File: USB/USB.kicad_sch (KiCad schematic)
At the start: 18 parts, among them J1 USBC-4-0-CX90MW9-24P1, U2 ESDA25L, U3 USB SWITCH 2CHANNEL TS3USB221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, U6 usb-polarity-TUSB321RWBR

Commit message: added TVS protection and filtering to CC lines
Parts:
- added TVS4: (no value), SPIRIT-footprints:1-channel-TVS-choke-XDFN6_1P2X1P2_ONS, symbol SPIRIT-components:TVS-choke-1-pair-EMI8141
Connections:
- net CC1: now also TVS4.1 (D+IN); no longer J2.1, Module1.94 (CC1)
- net CC2: now also TVS4.2 (D-IN); no longer J3.1, Module1.96 (CC2)
- net GND: now also TVS4.3 (GND), TVS4.4 (GND)
- net CC1f-jumpered: now reaches J2.2, U6.1 (CC1)
- net CC1f-jumpered: now also Module1.94 (CC1)
- net CC2f-jumpered: now reaches J3.2, U6.2 (CC2)
- net CC2f-jumpered: now also Module1.96 (CC2)
- new net CC1f: J2.1, TVS4.6 (D+OUT)
- new net CC2f: J3.1, TVS4.5 (D-OUT)
- no-connect marks 22 -> 30

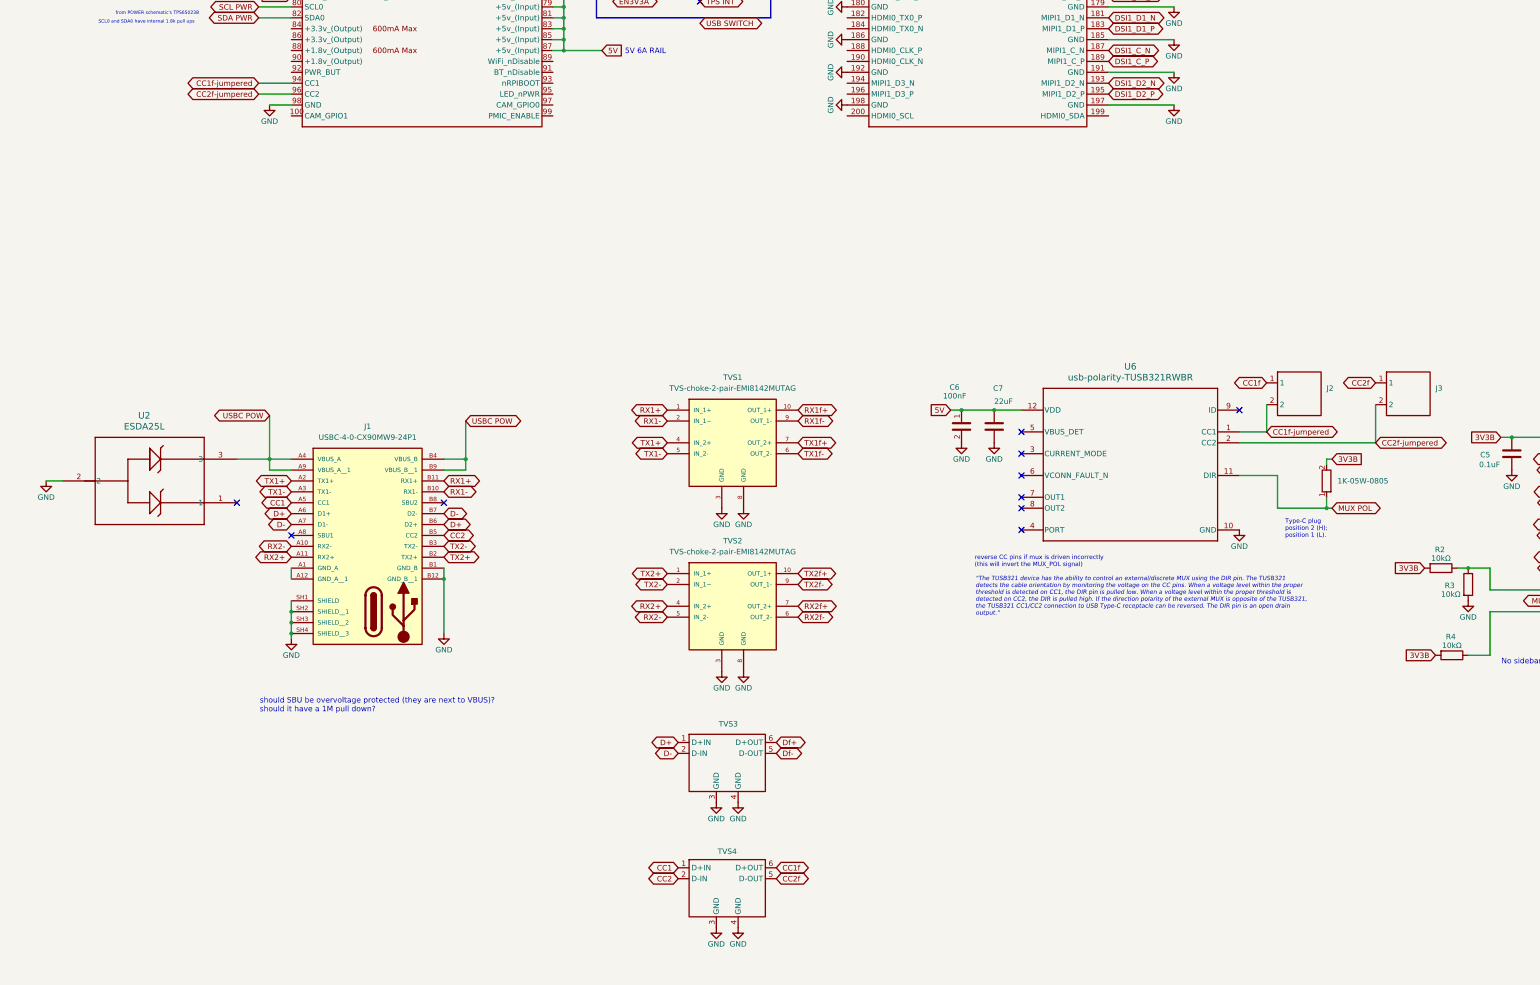
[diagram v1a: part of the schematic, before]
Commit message: fix TVS protection on CC lines
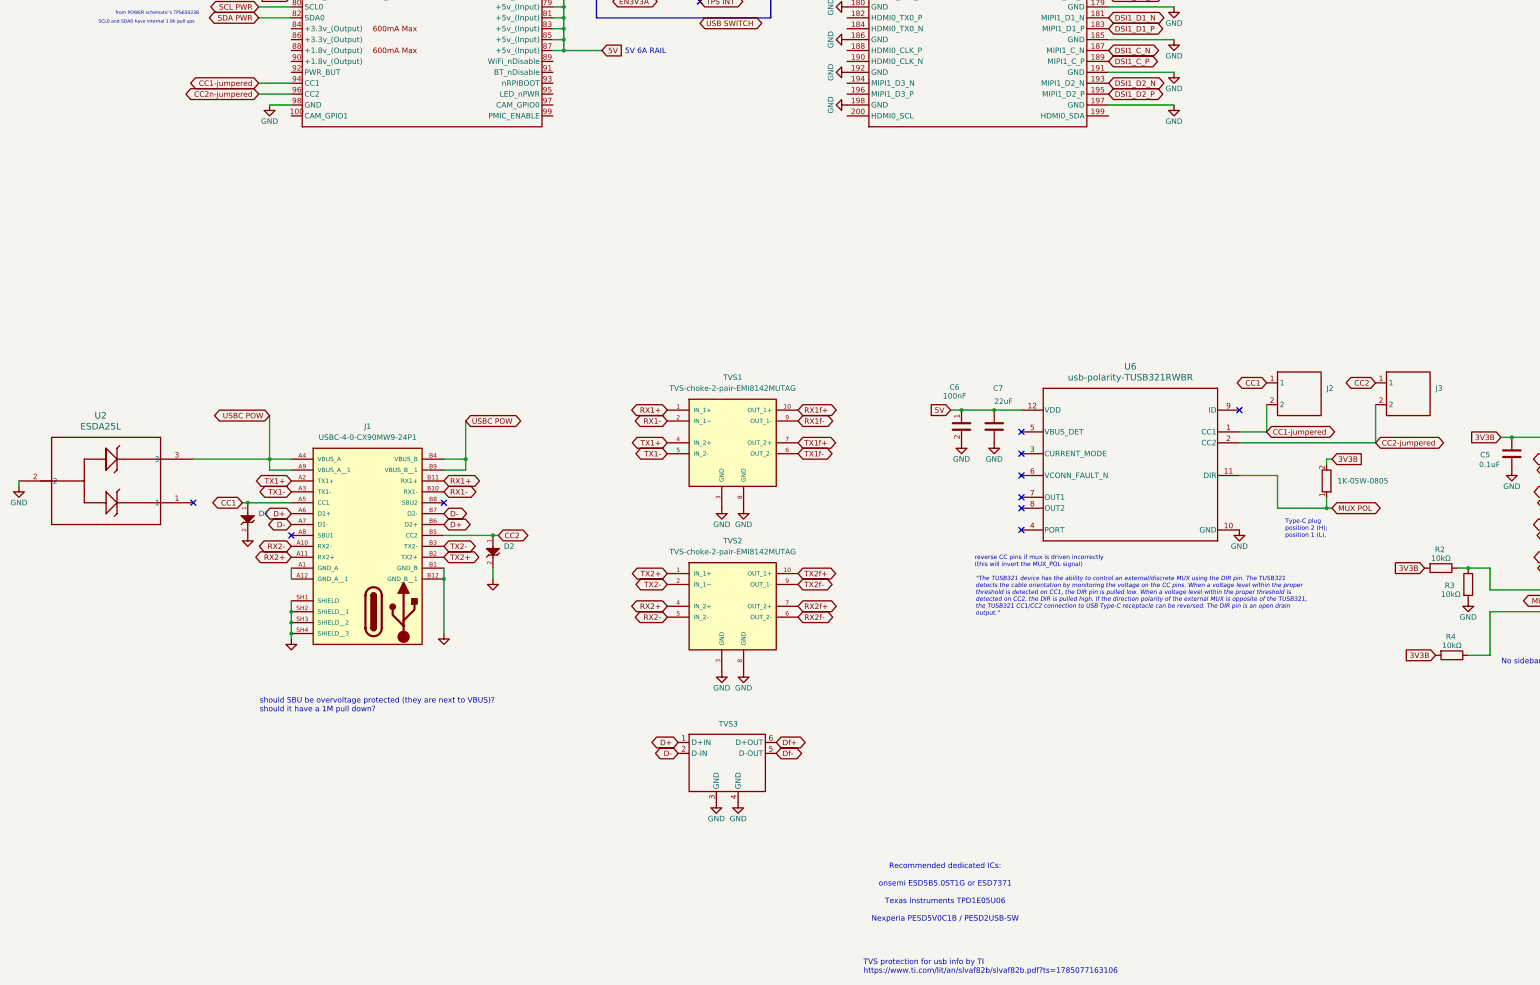
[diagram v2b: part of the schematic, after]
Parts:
- removed TVS4: (no value), SPIRIT-footprints:1-channel-TVS-choke-XDFN6_1P2X1P2_ONS, symbol SPIRIT-components:TVS-choke-1-pair-EMI8141
- added D1, D2: TPD1E05U06DPYR, CM5IO:TPD1E05U-SON65P60X100X45-2N, symbol SPIRIT-components:TPD1E05U06DPYR
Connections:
- net CC1f is gone; now on net CC1: J2.1
- net CC2f is gone; now on net CC2: J3.1
- net CC1: now also D1.1
- net CC2: now also D2.1
- net GND: now also D1.2, D2.2
- net CC1f-jumpered renamed CC1-jumpered
- net CC2f-jumpered renamed CC2-jumpered
- net CC2-jumpered: no longer Module1.96 (CC2)
- new net CC2n-jumpered: Module1.96 (CC2)
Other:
- note added: "Recommended dedicated ICs: onsemi ESD5B5.0ST1G or ESD7371 Texas Instruments TPD1E05U06 Nexperia PESD5V0C1B / PESD2USB-SW"
- note added: "TVS protection for usb info by TI https://www.ti.com/lit/an/slvaf82b/slvaf82b.pdf?ts=1785077163106"
- moved on the sheet: U2

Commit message: add lab power input headers
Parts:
- added J4: (no value), COMATEL THD:COMATEL_385.0358.1.02.400, symbol SPIRIT-components:2-pin-header
- J2, J3: footprint Connector_PinHeader_1.00mm:PinHeader_1x02_P1.00mm_Vertical -> COMATEL THD:COMATEL_385.0358.1.02.400
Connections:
- net CC2n-jumpered is gone; now on net CC2-jumpered: Module1.96 (CC2)
- net 3V3B: now also J4.1
- net 5V: now also J4.2
- no-connect marks 30 -> 33
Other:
- note added: "EXTERNAL POWER for testing purposes power from lab supply"
- note added: "TODO - add terminal block to power this (wago, 3V3, 5V, GND, DEBEUG?) // JUST SOLDER PADS - add patreons to silkscreen - remove unused labels - add test pads x- add pin header symbol for polarity flipper x- add 'lil chamfer to indicate orientation x- rename the diff pair nets to something with +- x- remove coupling caps as per cm5 datasheet"
- note removed: "TODO - add terminal block to power this (wago, 3V3, 5V, GND, DEBEUG?) // JUST SOLDER PADS - add patreons to silkscreen - remove unused labels x- add pin header symbol for polarity flipper x- add 'lil chamfer to indicate orientation x- rename the diff pair nets to something with +- x- remove coupling caps as per cm5 datasheet"
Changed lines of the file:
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@@
 		)
 	)
-	(text "TODO\n- add terminal block to power this (wago, 3V3, 5V, GND, DEBEUG?) // JUST SOLDER PADS\n- add patreons to silkscreen\n- remove unused labels\nx- add pin header symbol for polarity flipper\nx- add 'lil chamfer to indicate orientation\nx- rename the diff pair nets to something with +-\nx- remove coupling caps as per cm5 datasheet"
+	(text "TODO\n- add terminal block to power this (wago, 3V3, 5V, GND, DEBEUG?) // JUST SOLDER PADS\n- add patreons to silkscreen\n- remove unused labels\n- add test pads\nx- add pin header symbol for polarity flipper\nx- add 'lil chamfer to indicate orientation\nx- rename the diff pair nets to something with +-\nx- remove coupling caps as per cm5 datasheet"
 		(exclude_from_sim no)
 		(at 326.136 33.782 0)
@@
 		)
 	)
+	(text "EXTERNAL POWER\nfor testing purposes\npower from lab supply"
+		(exclude_from_sim no)
+		(at 498.856 331.47 0)
+		(effects
+			(font
+				(size 1.27 1.27)
+				(thickness 0.254)
+				(bold yes)
+			)
+		)
+	)
 	(text "use alt. function I2S0_SCLK\n\n"
 		(exclude_from_sim no)
@@
 	)
 	(no_connect
+		(at 156.21 176.53)
+	)
+	(no_connect
 		(at 251.46 289.56)
 	)
@@
 	)
 	(no_connect
+		(at 156.21 179.07)
+	)
+	(no_connect
 		(at 251.46 302.26)
 	)
@@
 	)
 	(no_connect
+		(at 156.21 173.99)
+	)
+	(no_connect
 		(at 420.37 308.61)
 	)
@@
 		)
 	)
+	(global_label "5V"
+		(shape input)
+		(at 492.76 345.44 180)
+		(fields_autoplaced yes)
+		(effects
+			(font
+				(size 1.27 1.27)
+			)
+			(justify right)
+		)
+		(property "Intersheetrefs" "${INTERSHEET_REFS}"
+			(at 487.4767 345.44 0)
+			(hide yes)
+			(show_name no)
+			(do_not_autoplace no)
+			(effects
+				(font
+					(size 1.27 1.27)
+				)
+				(justify right)
+			)
+		)
+	)
 	(global_label "RX1f-"
 		(shape bidirectional)
@@
 		)
 	)
-	(global_label "CC2n-jumpered"
+	(global_label "CC2-jumpered"
 		(shape bidirectional)
 		(at 73.66 200.66 180)
@@
 		)
 		(property "Intersheetrefs" "${INTERSHEET_REFS}"
-			(at 54.3841 200.66 0)
+			(at 55.5331 200.66 0)
 			(hide yes)
 			(show_name no)
@@
 	(global_label "USB SWITCH"
 		(shape bidirectional)
-		(at 176.53 184.15 0)
+		(at 176.53 185.42 0)
 		(fields_autoplaced yes)
 		(effects
@@
 		)
 		(property "Intersheetrefs" "${INTERSHEET_REFS}"
-			(at 192.2379 184.15 0)
+			(at 192.2379 185.42 0)
 			(hide yes)
 			(show_name no)
@@
 		)
 	)
+	(global_label "3V3B"
+		(shape input)
+		(at 492.76 340.36 180)
+		(fields_autoplaced yes)
+		(effects
+			(font
+				(size 1.27 1.27)
+			)
+			(justify right)
+		)
+		(property "Intersheetrefs" "${INTERSHEET_REFS}"
+			(at 484.9972 340.36 0)
+			(hide yes)
+			(show_name no)
+			(do_not_autoplace no)
+			(effects
+				(font
+					(size 1.27 1.27)
+				)
+				(justify right)
+			)
+		)
+	)
 	(global_label "USB SWITCH"
 		(shape bidirectional)
@@
 			)
 		)
-		(property "Footprint" "Connector_PinHeader_1.00mm:PinHeader_1x02_P1.00mm_Vertical"
+		(property "Footprint" "COMATEL THD:COMATEL_385.0358.1.02.400"
 			(at 316.23 262.89 0)
 			(hide yes)
@@
 			)
 		)
-		(property "Footprint" "Connector_PinHeader_1.00mm:PinHeader_1x02_P1.00mm_Vertical"
+		(property "Footprint" "COMATEL THD:COMATEL_385.0358.1.02.400"
 			(at 341.63 262.89 0)
 			(hide yes)
@@
 					(unit 1)
 				)
+			)
+		)
+	)
+	(symbol
+		(lib_id "SPIRIT-components:2-pin-header")
+		(at 500.38 342.9 0)
+		(unit 1)
+		(body_style 1)
+		(exclude_from_sim no)
+		(in_bom yes)
+		(on_board yes)
+		(in_pos_files yes)
+		(dnp no)
+		(fields_autoplaced yes)
+		(property "Reference" "J4"
+			(at 506.73 341.6299 0)
+			(show_name no)
+			(do_not_autoplace no)
+			(effects
+				(font
+					(size 1.27 1.27)
+				)
+				(justify left)
+			)
+		)
+		(property "Value" ""
+			(at 506.73 344.1699 0)
+			(show_name no)
+			(do_not_autoplace no)
+			(effects
+				(font
+					(size 1.27 1.27)
+				)
+				(justify left)
+			)
+		)
+		(property "Footprint" "COMATEL THD:COMATEL_385.0358.1.02.400"
+			(at 500.38 335.28 0)
+			(hide yes)
+			(show_name no)
+			(do_not_autoplace no)
+			(effects
+				(font
+					(size 1.27 1.27)
+				)
+			)
+		)
+		(property "Datasheet" ""
+			(at 500.38 335.28 0)
+			(hide yes)
+			(show_name no)
+			(do_not_autoplace no)
+			(effects
+				(font
+					(size 1.27 1.27)
+				)
+			)
+		)
+		(property "Description" ""
+			(at 500.38 335.28 0)
+			(hide yes)
+			(show_name no)
+			(do_not_autoplace no)
+			(effects
+				(font
+					(size 1.27 1.27)
+				)
+			)
+		)
+		(pin "2"
+		)
+		(pin "1"
+		)
+		(instances
+			(project "USB"
+				(path "/96ef50de-934d-4dd6-87fd-3fc40e345030"
+					(reference "J4")
+					(unit 1)
+				)

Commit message: connect VBUS to 25V TVS and CC to CM5 for tests
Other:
- note added: "V bus will probably never exceed 5V because cm5 is never negoatiating more that 5V 5A maybe the TVS should have a 5.5V working voltage"
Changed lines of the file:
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@@
+		)
+	)
+	(text "V bus will probably never exceed 5V\nbecause cm5 is never negoatiating more that 5V 5A\nmaybe the TVS should have a 5.5V working voltage"
+		(exclude_from_sim no)
+		(at 28.702 306.324 0)
+		(effects
+			(font
+				(size 1.27 1.27)
+			)
 		)
 	)

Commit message: add test points for USB SWITCH and MUX POL
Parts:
- added J5: (no value), COMATEL THD:COMATEL_385.0358.1.02.400, symbol SPIRIT-components:2-pin-header
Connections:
- net MUX POL: now also J5.2
- net USB SWITCH: now also J5.1
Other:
- note added: "TEST POINT"
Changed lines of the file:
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@@
 		)
 	)
+	(text "TEST POINT"
+		(exclude_from_sim no)
+		(at 539.242 331.47 0)
+		(effects
+			(font
+				(size 1.27 1.27)
+				(thickness 0.254)
+				(bold yes)
+			)
+		)
+	)
 	(text "Recommended dedicated ICs:\n\nonsemi ESD5B5.0ST1G or ESD7371\n\nTexas Instruments TPD1E05U06\n\nNexperia PESD5V0C1B / PESD2USB-SW"
 		(exclude_from_sim no)
@@
 	(global_label "USB SWITCH"
 		(shape bidirectional)
-		(at 176.53 185.42 0)
+		(at 533.4 340.36 180)
 		(fields_autoplaced yes)
 		(effects
@@
 				(size 1.27 1.27)
 			)
-			(justify left)
+			(justify right)
 		)
 		(property "Intersheetrefs" "${INTERSHEET_REFS}"
-			(at 192.2379 185.42 0)
+			(at 517.6921 340.36 0)
 			(hide yes)
 			(show_name no)
@@
 					(size 1.27 1.27)
 				)
-				(justify left)
+				(justify right)
 			)
 		)
@@
 		)
 	)
+	(global_label "MUX POL"
+		(shape bidirectional)
+		(at 533.4 345.44 180)
+		(fields_autoplaced yes)
+		(effects
+			(font
+				(size 1.27 1.27)
+			)
+			(justify right)
+		)
+		(property "Intersheetrefs" "${INTERSHEET_REFS}"
+			(at 520.7159 345.44 0)
+			(hide yes)
+			(show_name no)
+			(do_not_autoplace no)
+			(effects
+				(font
+					(size 1.27 1.27)
+				)
+				(justify right)
+			)
+		)
+	)
 	(global_label "DIS_SCL"
 		(shape output)
@@
 					(unit 1)
 				)
+			)
+		)
+	)
+	(symbol
+		(lib_id "SPIRIT-components:2-pin-header")
+		(at 541.02 342.9 0)
+		(unit 1)
+		(body_style 1)
+		(exclude_from_sim no)
+		(in_bom yes)
+		(on_board yes)
+		(in_pos_files yes)
+		(dnp no)
+		(fields_autoplaced yes)
+		(property "Reference" "J5"
+			(at 547.37 341.6299 0)
+			(show_name no)
+			(do_not_autoplace no)
+			(effects
+				(font
+					(size 1.27 1.27)
+				)
+				(justify left)
+			)
+		)
+		(property "Value" ""
+			(at 547.37 344.1699 0)
+			(show_name no)
+			(do_not_autoplace no)
+			(effects
+				(font
+					(size 1.27 1.27)
+				)
+				(justify left)
+			)
+		)
+		(property "Footprint" "COMATEL THD:COMATEL_385.0358.1.02.400"
+			(at 541.02 335.28 0)
+			(hide yes)
+			(show_name no)
+			(do_not_autoplace no)
+			(effects
+				(font
+					(size 1.27 1.27)
+				)
+			)
+		)
+		(property "Datasheet" ""
+			(at 541.02 335.28 0)
+			(hide yes)
+			(show_name no)
+			(do_not_autoplace no)
+			(effects
+				(font
+					(size 1.27 1.27)
+				)
+			)
+		)
+		(property "Description" ""
+			(at 541.02 335.28 0)
+			(hide yes)
+			(show_name no)
+			(do_not_autoplace no)
+			(effects
+				(font
+					(size 1.27 1.27)
+				)
+			)
+		)
+		(pin "2"
+		)
+		(pin "1"
+		)
+		(instances
+			(project "USB"
+				(path "/96ef50de-934d-4dd6-87fd-3fc40e345030"
+					(reference "J5")
+					(unit 1)
+				)

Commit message: connect test points and connect CM5 to plane
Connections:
- net GND: now also Module1.59 (GND), Module1.7 (GND)
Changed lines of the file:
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@@
+	)
+	(symbol
+		(lib_name "GND_37")
+		(lib_id "power:GND")
+		(at 142.24 88.9 90)
+		(unit 1)
+		(body_style 1)
+		(exclude_from_sim no)
+		(in_bom yes)
+		(on_board yes)
+		(in_pos_files yes)
+		(dnp no)
+		(property "Reference" "#PWR069"
+			(at 148.59 88.9 0)
+			(hide yes)
+			(show_name no)
+			(do_not_autoplace no)
+			(effects
+				(font
+					(size 1.27 1.27)
+				)
+			)
+		)
+		(property "Value" "GND"
+			(at 146.05 88.9 0)
+			(show_name no)
+			(do_not_autoplace no)
+			(effects
+				(font
+					(size 1.27 1.27)
+				)
+			)
+		)
+		(property "Footprint" ""
+			(at 142.24 88.9 0)
+			(hide yes)
+			(show_name no)
+			(do_not_autoplace no)
+			(effects
+				(font
+					(size 1.27 1.27)
+				)
+			)
+		)
+		(property "Datasheet" ""
+			(at 142.24 88.9 0)
+			(hide yes)
+			(show_name no)
+			(do_not_autoplace no)
+			(effects
+				(font
+					(size 1.27 1.27)
+				)
+			)
+		)
+		(property "Description" ""
+			(at 142.24 88.9 0)
+			(hide yes)
+			(show_name no)
+			(do_not_autoplace no)
+			(effects
+				(font
+					(size 1.27 1.27)
+				)
+			)
+		)
+		(pin "1"
+		)
+		(instances
+			(project "USB"
+				(path "/96ef50de-934d-4dd6-87fd-3fc40e345030"
+					(reference "#PWR069")
+					(unit 1)
+				)
+			)
+		)
 	)
 	(symbol
@@
 					(unit 1)
 				)
+			)
+		)
+	)
+	(symbol
+		(lib_name "GND_4")
+		(lib_id "power:GND")
+		(at 142.24 154.94 90)
+		(unit 1)
+		(body_style 1)
+		(exclude_from_sim no)
+		(in_bom yes)
+		(on_board yes)
+		(in_pos_files yes)
+		(dnp no)
+		(property "Reference" "#PWR056"
+			(at 148.59 154.94 0)
+			(hide yes)
+			(show_name no)
+			(do_not_autoplace no)
+			(effects
+				(font
+					(size 1.27 1.27)
+				)
+			)
+		)
+		(property "Value" "GND"
+			(at 146.05 154.94 0)
+			(show_name no)
+			(do_not_autoplace no)
+			(effects
+				(font
+					(size 1.27 1.27)
+				)
+			)
+		)
+		(property "Footprint" ""
+			(at 142.24 154.94 0)
+			(hide yes)
+			(show_name no)
+			(do_not_autoplace no)
+			(effects
+				(font
+					(size 1.27 1.27)
+				)
+			)
+		)
+		(property "Datasheet" ""
+			(at 142.24 154.94 0)
+			(hide yes)
+			(show_name no)
+			(do_not_autoplace no)
+			(effects
+				(font
+					(size 1.27 1.27)
+				)
+			)
+		)
+		(property "Description" ""
+			(at 142.24 154.94 0)
+			(hide yes)
+			(show_name no)
+			(do_not_autoplace no)
+			(effects
+				(font
+					(size 1.27 1.27)
+				)
+			)
+		)
+		(pin "1"
+		)
+		(instances
+			(project "USB"
+				(path "/96ef50de-934d-4dd6-87fd-3fc40e345030"
+					(reference "#PWR056")
+					(unit 1)
+				)

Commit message: stitching vias along SS lines
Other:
- note added: "Stitching via spacing math (1/20) * ((3*10^8)/(sqrt(4.6)*2.4*10^9)) ans = 2.9141e-03"
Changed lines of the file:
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@@
+		)
+	)
+	(text "Stitching via spacing math\n(1/20) * ((3*10^8)/(sqrt(4.6)*2.4*10^9))\nans = 2.9141e-03"
+		(exclude_from_sim no)
+		(at 416.814 384.556 0)
+		(effects
+			(font
+				(size 1.27 1.27)
+			)
+			(justify left)
 		)
 	)

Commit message: tune and stitch d+,d- lines, connect AGND of type c socket to GND
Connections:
- net GND: now also J1.A1 (GND_A), J1.A12 (GND_A__1)
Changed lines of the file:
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@@
 	)
 	(junction
+		(at 81.28 313.69)
+		(diameter 0)
+		(color 0 0 0 0)
+	)
+	(junction
 		(at 81.28 321.31)
 		(diameter 0)
@@
 					(unit 1)
 				)
+			)
+		)
+	)
+	(symbol
+		(lib_id "power:GND")
+		(at 81.28 313.69 0)
+		(unit 1)
+		(body_style 1)
+		(exclude_from_sim no)
+		(in_bom yes)
+		(on_board yes)
+		(in_pos_files yes)
+		(dnp no)
+		(property "Reference" "#PWR070"
+			(at 81.28 320.04 0)
+			(hide yes)
+			(show_name no)
+			(do_not_autoplace no)
+			(effects
+				(font
+					(size 1.27 1.27)
+				)
+			)
+		)
+		(property "Value" "GND"
+			(at 81.28 317.5 0)
+			(hide yes)
+			(show_name no)
+			(do_not_autoplace no)
+			(effects
+				(font
+					(size 1.27 1.27)
+				)
+			)
+		)
+		(property "Footprint" ""
+			(at 81.28 313.69 0)
+			(hide yes)
+			(show_name no)
+			(do_not_autoplace no)
+			(effects
+				(font
+					(size 1.27 1.27)
+				)
+			)
+		)
+		(property "Datasheet" ""
+			(at 81.28 313.69 0)
+			(hide yes)
+			(show_name no)
+			(do_not_autoplace no)
+			(effects
+				(font
+					(size 1.27 1.27)
+				)
+			)
+		)
+		(property "Description" ""
+			(at 81.28 313.69 0)
+			(hide yes)
+			(show_name no)
+			(do_not_autoplace no)
+			(effects
+				(font
+					(size 1.27 1.27)
+				)
+			)
+		)
+		(pin "1"
+		)
+		(instances
+			(project "USB"
+				(path "/96ef50de-934d-4dd6-87fd-3fc40e345030"
+					(reference "#PWR070")
+					(unit 1)
+				)
